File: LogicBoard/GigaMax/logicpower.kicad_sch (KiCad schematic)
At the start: 13 parts, among them U16 TPS5430DDAR, U9 AMS1117-3.3

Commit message: moved libs and gigamax version
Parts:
- C32, C33, C34, C8: footprint Capacitor_SMD:C_1206_3216Metric -> Capacitor_SMD:C_0805_2012Metric; MPN C12891 -> C45783
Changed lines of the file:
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@@
     (pin "1")
     (instances
-      (project "DevKit"
+      (project "GigaMax"
         (path "/768a484b-8a27-40cf-8cad-0f63935b1af0"
           (reference "#PWR08") (unit 1)
@@
     (pin "1")
     (instances
-      (project "DevKit"
+      (project "GigaMax"
         (path "/768a484b-8a27-40cf-8cad-0f63935b1af0"
           (reference "#PWR08") (unit 1)
@@
     (pin "2")
     (instances
-      (project "DevKit"
+      (project "GigaMax"
         (path "/768a484b-8a27-40cf-8cad-0f63935b1af0/717cb4b7-b47a-435c-946f-7c938a1d7e5f"
           (reference "D9") (unit 1)
@@
       (effects (font (size 1.27 1.27)) (justify left))
     )
-    (property "Footprint" "Capacitor_SMD:C_1206_3216Metric" (at 220.6752 100.33 0)
+    (property "Footprint" "Capacitor_SMD:C_0805_2012Metric" (at 220.6752 100.33 0)
       (effects (font (size 1.27 1.27)) hide)
     )
@@
       (effects (font (size 1.27 1.27)) hide)
     )
-    (property "MPN" "C12891" (at 219.71 96.52 0)
-      (effects (font (size 1.27 1.27)) hide)
-    )
-    (pin "1")
-    (pin "2")
-    (instances
-      (project "DevKit"
+    (property "MPN" "C45783" (at 219.71 96.52 0)
+      (effects (font (size 1.27 1.27)) hide)
+    )
+    (pin "1")
+    (pin "2")
+    (instances
+      (project "GigaMax"
         (path "/768a484b-8a27-40cf-8cad-0f63935b1af0/717cb4b7-b47a-435c-946f-7c938a1d7e5f"
           (reference "C33") (unit 1)
@@
     (pin "1")
     (instances
-      (project "DevKit"
+      (project "GigaMax"
         (path "/768a484b-8a27-40cf-8cad-0f63935b1af0/717cb4b7-b47a-435c-946f-7c938a1d7e5f"
           (reference "#FLG02") (unit 1)
@@
     (pin "1")
     (instances
-      (project "DevKit"
+      (project "GigaMax"
         (path "/768a484b-8a27-40cf-8cad-0f63935b1af0"
           (reference "#PWR08") (unit 1)
@@
     (pin "1")
     (instances
-      (project "DevKit"
+      (project "GigaMax"
         (path "/768a484b-8a27-40cf-8cad-0f63935b1af0"
           (reference "#PWR08") (unit 1)
@@
     (pin "2")
     (instances
-      (project "DevKit"
+      (project "GigaMax"
         (path "/768a484b-8a27-40cf-8cad-0f63935b1af0/717cb4b7-b47a-435c-946f-7c938a1d7e5f"
           (reference "C54") (unit 1)
@@
     (pin "1")
     (instances
-      (project "DevKit"
+      (project "GigaMax"
         (path "/768a484b-8a27-40cf-8cad-0f63935b1af0"
           (reference "#PWR08") (unit 1)
@@
     (pin "1")
     (instances
-      (project "DevKit"
+      (project "GigaMax"
         (path "/768a484b-8a27-40cf-8cad-0f63935b1af0"
           (reference "#PWR08") (unit 1)
@@
     (pin "1")
     (instances
-      (project "DevKit"
+      (project "GigaMax"
         (path "/768a484b-8a27-40cf-8cad-0f63935b1af0"
           (reference "#PWR03") (unit 1)
@@
     (pin "1")
     (instances
-      (project "DevKit"
+      (project "GigaMax"
         (path "/768a484b-8a27-40cf-8cad-0f63935b1af0/717cb4b7-b47a-435c-946f-7c938a1d7e5f"
           (reference "#PWR074") (unit 1)
@@
     (pin "3")
     (instances
-      (project "DevKit"
+      (project "GigaMax"
         (path "/768a484b-8a27-40cf-8cad-0f63935b1af0/717cb4b7-b47a-435c-946f-7c938a1d7e5f"
           (reference "U9") (unit 1)
@@
     (pin "1")
     (instances
-      (project "DevKit"
+      (project "GigaMax"
         (path "/768a484b-8a27-40cf-8cad-0f63935b1af0"
           (reference "#PWR08") (unit 1)
@@
       (effects (font (size 1.27 1.27)) (justify left))
     )
-    (property "Footprint" "Capacitor_SMD:C_1206_3216Metric" (at 155.9052 99.06 0)
+    (property "Footprint" "Capacitor_SMD:C_0805_2012Metric" (at 155.9052 99.06 0)
       (effects (font (size 1.27 1.27)) hide)
     )
@@
       (effects (font (size 1.27 1.27)) hide)
     )
-    (property "MPN" "C12891" (at 154.94 95.25 0)
-      (effects (font (size 1.27 1.27)) hide)
-    )
-    (pin "1")
-    (pin "2")
-    (instances
-      (project "DevKit"
+    (property "MPN" "C45783" (at 154.94 95.25 0)
+      (effects (font (size 1.27 1.27)) hide)
+    )
+    (pin "1")
+    (pin "2")
+    (instances
+      (project "GigaMax"
         (path "/768a484b-8a27-40cf-8cad-0f63935b1af0/717cb4b7-b47a-435c-946f-7c938a1d7e5f"
           (reference "C34") (unit 1)
@@
     (pin "9")
     (instances
-      (project "DevKit"
+      (project "GigaMax"
         (path "/768a484b-8a27-40cf-8cad-0f63935b1af0/717cb4b7-b47a-435c-946f-7c938a1d7e5f"
           (reference "U16") (unit 1)
@@
       (effects (font (size 1.27 1.27)) (justify left))
     )
-    (property "Footprint" "Capacitor_SMD:C_1206_3216Metric" (at 61.9252 99.06 0)
+    (property "Footprint" "Capacitor_SMD:C_0805_2012Metric" (at 61.9252 99.06 0)
       (effects (font (size 1.27 1.27)) hide)
     )
@@
       (effects (font (size 1.27 1.27)) hide)
     )
-    (property "MPN" "C12891" (at 60.96 95.25 0)
-      (effects (font (size 1.27 1.27)) hide)
-    )
-    (pin "1")
-    (pin "2")
-    (instances
-      (project "DevKit"
+    (property "MPN" "C45783" (at 60.96 95.25 0)
+      (effects (font (size 1.27 1.27)) hide)
+    )
+    (pin "1")
+    (pin "2")
+    (instances
+      (project "GigaMax"
         (path "/768a484b-8a27-40cf-8cad-0f63935b1af0"
           (reference "C8") (unit 1)
@@
     (pin "1")
     (instances
-      (project "DevKit"
+      (project "GigaMax"
         (path "/768a484b-8a27-40cf-8cad-0f63935b1af0/717cb4b7-b47a-435c-946f-7c938a1d7e5f"
           (reference "#FLG01") (unit 1)
@@
     (pin "1")
     (instances
-      (project "DevKit"
+      (project "GigaMax"
         (path "/768a484b-8a27-40cf-8cad-0f63935b1af0"
           (reference "#PWR08") (unit 1)
@@
     (pin "2")
     (instances
-      (project "DevKit"
+      (project "GigaMax"
         (path "/768a484b-8a27-40cf-8cad-0f63935b1af0/717cb4b7-b47a-435c-946f-7c938a1d7e5f"
           (reference "R46") (unit 1)
@@
       (effects (font (size 1.27 1.27)) (justify left))
     )
-    (property "Footprint" "Capacitor_SMD:C_1206_3216Metric" (at 191.4652 100.33 0)
+    (property "Footprint" "Capacitor_SMD:C_0805_2012Metric" (at 191.4652 100.33 0)
       (effects (font (size 1.27 1.27)) hide)
     )
@@
       (effects (font (size 1.27 1.27)) hide)
     )
-    (property "MPN" "C12891" (at 190.5 96.52 0)
-      (effects (font (size 1.27 1.27)) hide)
-    )
-    (pin "1")
-    (pin "2")
-    (instances
-      (project "DevKit"
+    (property "MPN" "C45783" (at 190.5 96.52 0)
+      (effects (font (size 1.27 1.27)) hide)
+    )
+    (pin "1")
+    (pin "2")
+    (instances
+      (project "GigaMax"
         (path "/768a484b-8a27-40cf-8cad-0f63935b1af0/717cb4b7-b47a-435c-946f-7c938a1d7e5f"
           (reference "C32") (unit 1)
@@
     (pin "2")
     (instances
-      (project "DevKit"
+      (project "GigaMax"
         (path "/768a484b-8a27-40cf-8cad-0f63935b1af0/717cb4b7-b47a-435c-946f-7c938a1d7e5f"
           (reference "C31") (unit 1)
@@
     (pin "1")
     (instances
-      (project "DevKit"
+      (project "GigaMax"
         (path "/768a484b-8a27-40cf-8cad-0f63935b1af0/717cb4b7-b47a-435c-946f-7c938a1d7e5f"
           (reference "#PWR072") (unit 1)
@@
     (pin "1")
     (instances
-      (project "DevKit"
+      (project "GigaMax"
         (path "/768a484b-8a27-40cf-8cad-0f63935b1af0/717cb4b7-b47a-435c-946f-7c938a1d7e5f"
           (reference "#FLG03") (unit 1)
@@
     (pin "1")
     (instances
-      (project "DevKit"
+      (project "GigaMax"
         (path "/768a484b-8a27-40cf-8cad-0f63935b1af0"
           (reference "#PWR08") (unit 1)
@@
     (pin "1")
     (instances
-      (project "DevKit"
+      (project "GigaMax"
         (path "/768a484b-8a27-40cf-8cad-0f63935b1af0/717cb4b7-b47a-435c-946f-7c938a1d7e5f"
           (reference "#PWR071") (unit 1)
@@
     (pin "2")
     (instances
-      (project "DevKit"
+      (project "GigaMax"
         (path "/768a484b-8a27-40cf-8cad-0f63935b1af0"
           (reference "R47") (unit 1)
@@
     (pin "2")
     (instances
-      (project "DevKit"
+      (project "GigaMax"
         (path "/768a484b-8a27-40cf-8cad-0f63935b1af0/717cb4b7-b47a-435c-946f-7c938a1d7e5f"
           (reference "C30") (unit 1)
@@
     (pin "1")
     (instances
-      (project "DevKit"
+      (project "GigaMax"
         (path "/768a484b-8a27-40cf-8cad-0f63935b1af0"
           (reference "#PWR08") (unit 1)
@@
     (pin "2")
     (instances
-      (project "DevKit"
+      (project "GigaMax"
         (path "/768a484b-8a27-40cf-8cad-0f63935b1af0/717cb4b7-b47a-435c-946f-7c938a1d7e5f"
           (reference "L2") (unit 1)

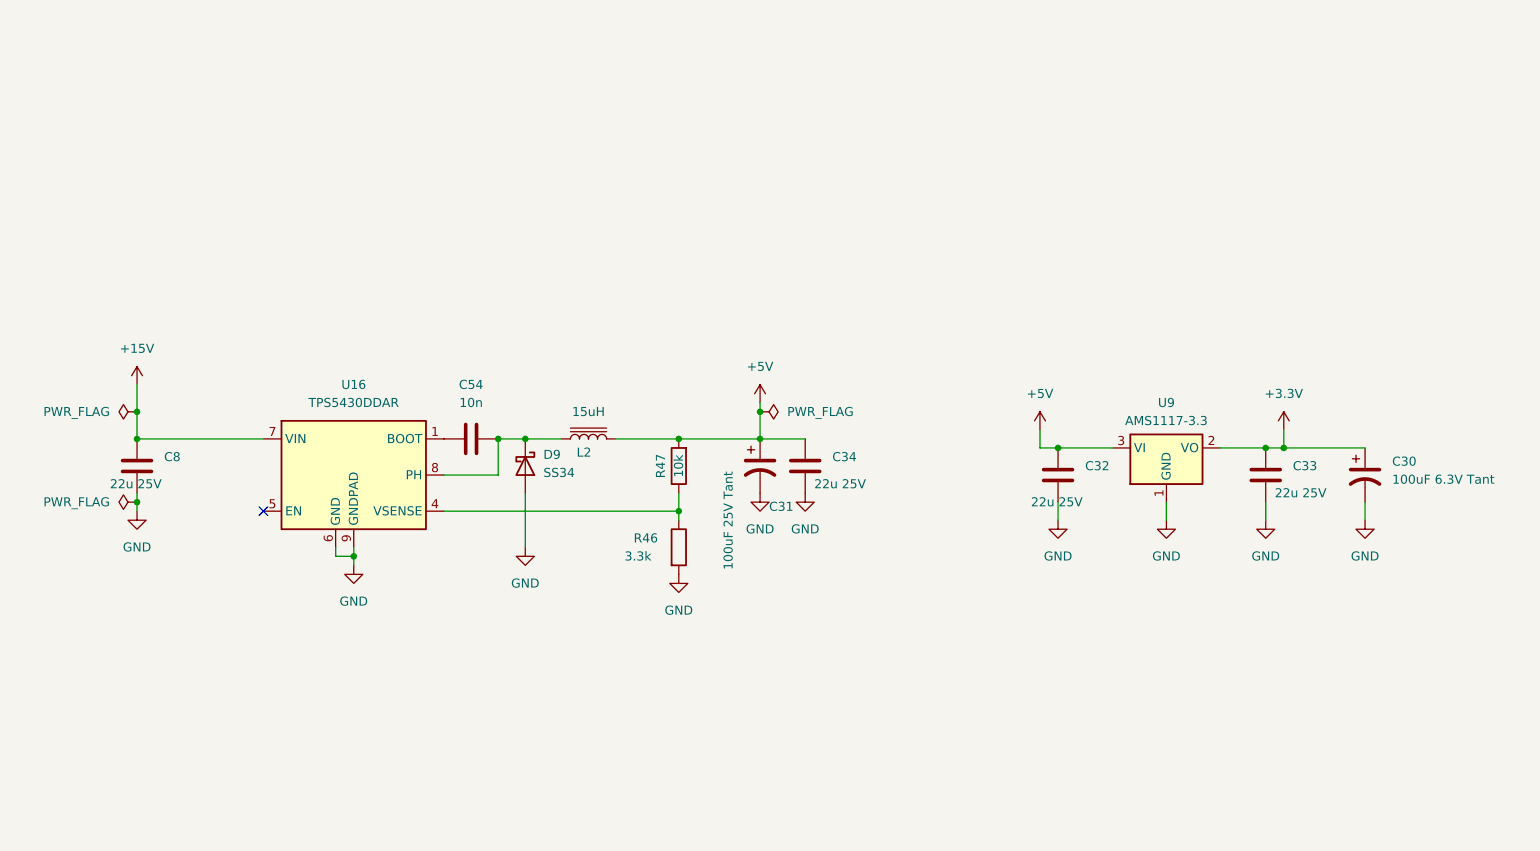
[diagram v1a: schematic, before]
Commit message: v2.8.0 - Small Hall sensors
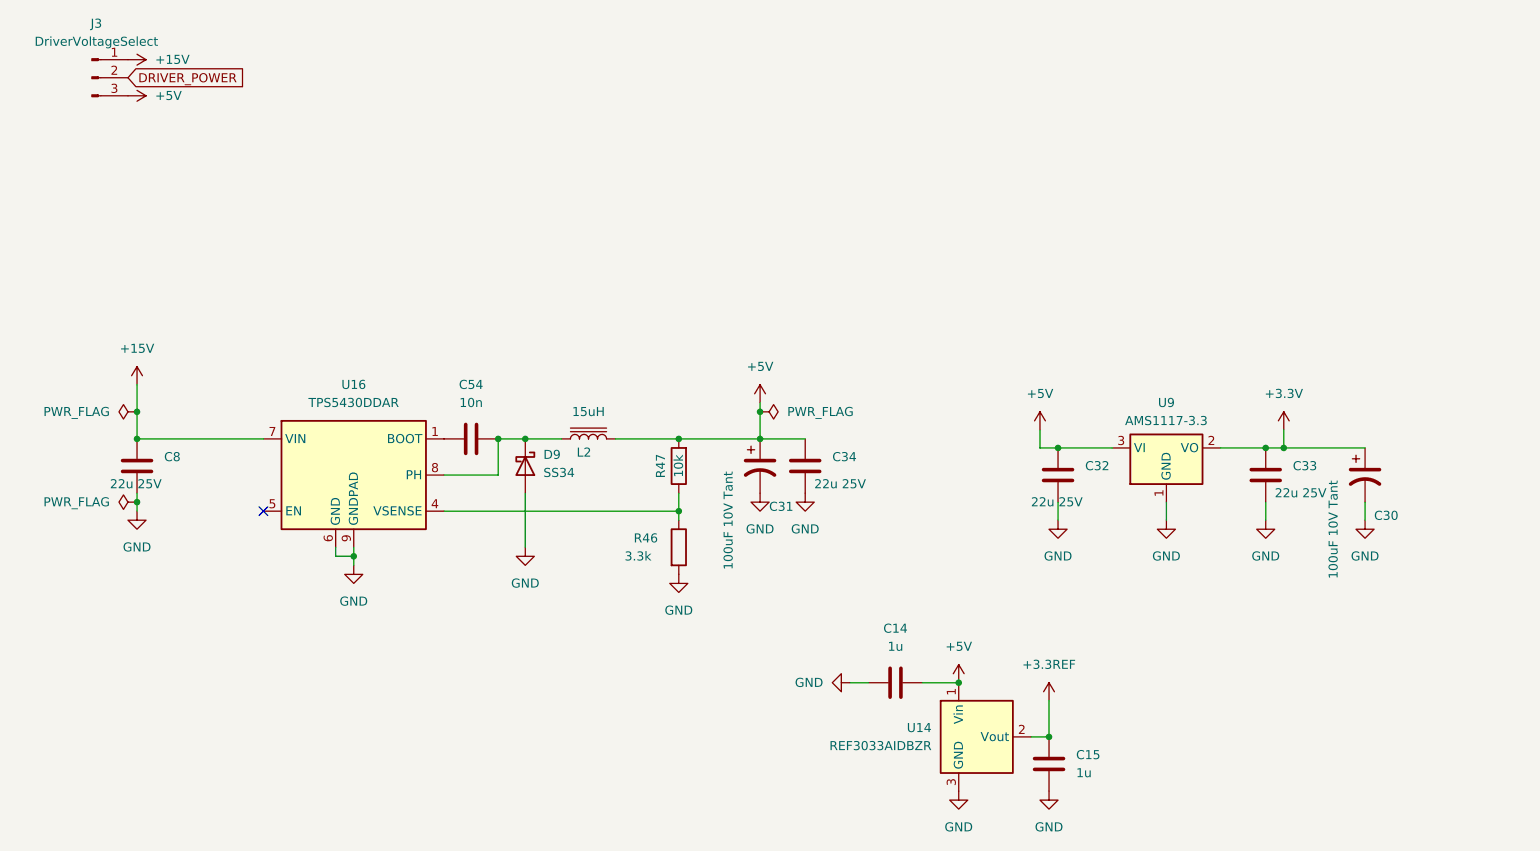
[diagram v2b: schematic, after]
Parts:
- added C14, C15: 1u, GigaVescLibs:C_0603_1608Metric_L, symbol Device:C
- added J3: DriverVoltageSelect, Connector_PinHeader_2.54mm:PinHeader_1x03_P2.54mm_Vertical, symbol Connector:Conn_01x03_Pin
- added U14: REF3033AIDBZR, Package_TO_SOT_SMD:SOT-23, symbol Reference_Voltage:ISL21070CIH320Z-TK
- C30: value 100uF 6.3V Tant -> 100uF 10V Tant; footprint Capacitor_Tantalum_SMD:CP_EIA-3528-15_AVX-H -> Capacitor_Tantalum_SMD:CP_EIA-6032-28_Kemet-C; JLCRotOffset (none) -> -180; MPN C16133 -> C171664
- C31: value 100uF 25V Tant -> 100uF 10V Tant; footprint Capacitor_Tantalum_SMD:CP_EIA-7343-31_Kemet-D -> Capacitor_Tantalum_SMD:CP_EIA-6032-28_Kemet-C; JLCRotOffset (none) -> -180; MPN C212710 -> C171664
- C32, C33, C34, C8: footprint Capacitor_SMD:C_0805_2012Metric -> Capacitor_SMD:C_1206_3216Metric; MPN C45783 -> C12891
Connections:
- net +15V: now also J3.1 (Pin_1)
- net +5V: now also C14.1, J3.3 (Pin_3), U14.1 (Vin)
- net GND: now also C14.2, C15.2, U14.3 (GND)
- new net +3.3REF: C15.1, U14.2 (Vout)
- new net DRIVER_POWER: J3.2 (Pin_2)
